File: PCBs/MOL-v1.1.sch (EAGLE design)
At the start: 67 parts, among them IC1 ULN2803, IC2 ULN2803, J1 SERVO 1, J2 SERVO 2, U1 SN74LVC2G04DBV, U2 JOYSTICKPTH, U3 JOYSTICKPTH

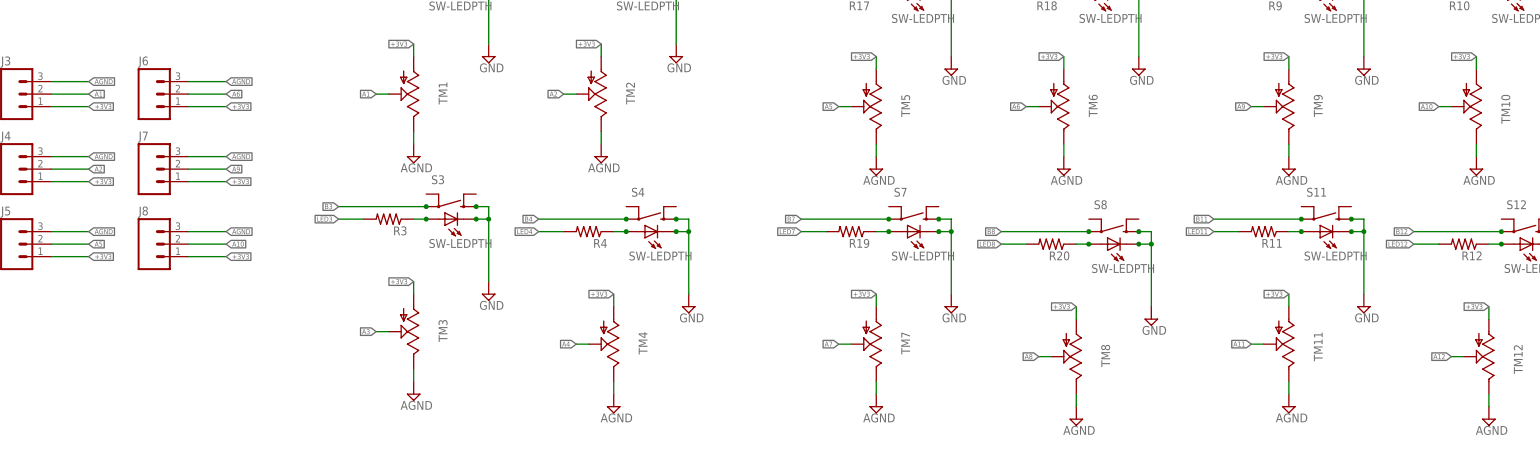
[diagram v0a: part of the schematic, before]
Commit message: signal name changes in MOL PCB v1.1
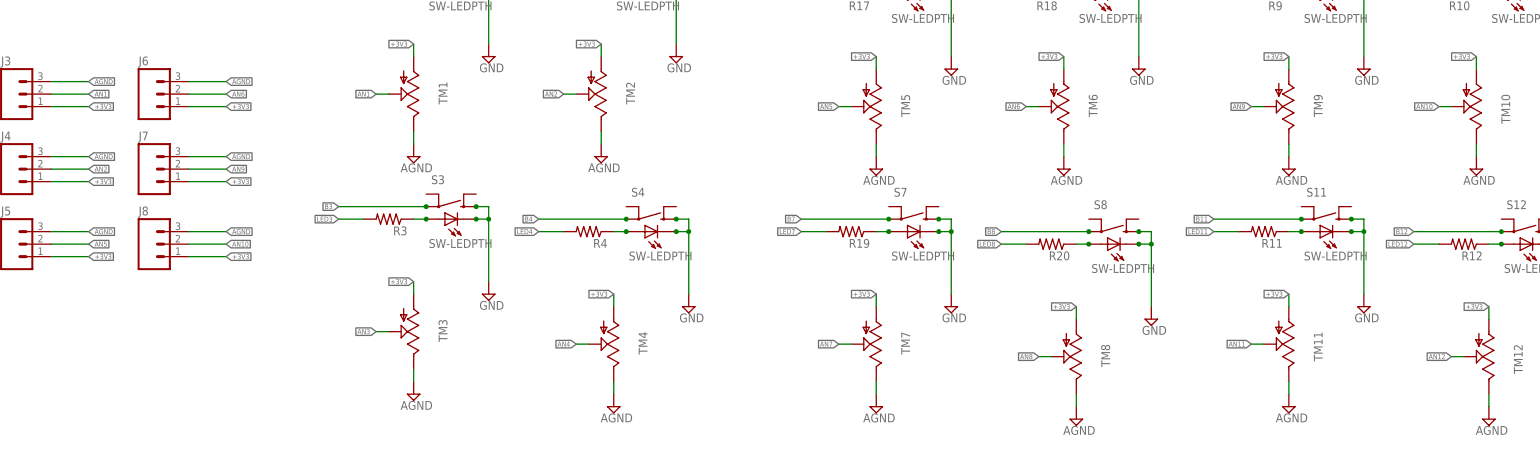
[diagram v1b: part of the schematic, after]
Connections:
- removed net A1: J3.2, TM1.S
- removed net A10: J8.2, TM10.S
- removed net A11: TM11.S
- removed net A12: TM12.S
- removed net A2: J4.2, TM2.S
- removed net A3: TM3.S
- removed net A4: TM4.S
- removed net A5: J5.2, TM5.S
- removed net A6: J6.2, TM6.S
- removed net A7: TM7.S
- removed net A8: TM8.S
- removed net A9: J7.2, TM9.S
- net AN1: now also J3.2, TM1.S
- net AN10: now also J8.2, TM10.S
- net AN11: now also TM11.S
- net AN12: now also TM12.S
- net AN2: now also J4.2, TM2.S
- net AN3: now also TM3.S
- net AN4: now also TM4.S
- net AN5: now also J5.2, TM5.S
- net AN6: now also J6.2, TM6.S
- net AN7: now also TM7.S
- net AN8: now also TM8.S
- net AN9: now also J7.2, TM9.S
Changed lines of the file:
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@@
-</segment>
-</net>
-<net name="A1" class="3">
-<segment>
-<pinref part="TM1" gate="G$1" pin="S"/>
-<wire x1="-83.82" y1="-81.28" x2="-86.36" y2="-81.28" width="0.1524" layer="91"/>
-<label x="-86.36" y="-81.28" size="1.016" layer="95" rot="R180" xref="yes"/>
-</segment>
-<segment>
-<pinref part="J3" gate="G$1" pin="2"/>
-<wire x1="-152.4" y1="-81.28" x2="-144.78" y2="-81.28" width="0.1524" layer="91"/>
-<label x="-144.78" y="-81.28" size="1.016" layer="95" xref="yes"/>
-</segment>
-</net>
-<net name="A2" class="3">
-<segment>
-<pinref part="TM2" gate="G$1" pin="S"/>
-<wire x1="-45.72" y1="-81.28" x2="-48.26" y2="-81.28" width="0.1524" layer="91"/>
-<label x="-48.26" y="-81.28" size="1.016" layer="95" rot="R180" xref="yes"/>
-</segment>
-<segment>
-<pinref part="J4" gate="G$1" pin="2"/>
-<wire x1="-152.4" y1="-96.52" x2="-144.78" y2="-96.52" width="0.1524" layer="91"/>
-<label x="-144.78" y="-96.52" size="1.016" layer="95" xref="yes"/>
-</segment>
-</net>
-<net name="A3" class="3">
-<segment>
-<pinref part="TM3" gate="G$1" pin="S"/>
-<wire x1="-83.82" y1="-129.54" x2="-86.36" y2="-129.54" width="0.1524" layer="91"/>
-<label x="-86.36" y="-129.54" size="1.016" layer="95" rot="R180" xref="yes"/>
-</segment>
-</net>
-<net name="A4" class="3">
-<segment>
-<pinref part="TM4" gate="G$1" pin="S"/>
-<wire x1="-43.18" y1="-132.08" x2="-45.72" y2="-132.08" width="0.1524" layer="91"/>
-<label x="-45.72" y="-132.08" size="1.016" layer="95" rot="R180" xref="yes"/>
-</segment>
-</net>
-<net name="A5" class="3">
-<segment>
-<pinref part="TM5" gate="G$1" pin="S"/>
-<wire x1="10.16" y1="-83.82" x2="7.62" y2="-83.82" width="0.1524" layer="91"/>
-<label x="7.62" y="-83.82" size="1.016" layer="95" rot="R180" xref="yes"/>
-</segment>
-<segment>
-<pinref part="J5" gate="G$1" pin="2"/>
-<wire x1="-152.4" y1="-111.76" x2="-144.78" y2="-111.76" width="0.1524" layer="91"/>
-<label x="-144.78" y="-111.76" size="1.016" layer="95" xref="yes"/>
-</segment>
-</net>
-<net name="A6" class="3">
-<segment>
-<pinref part="TM6" gate="G$1" pin="S"/>
-<wire x1="48.26" y1="-83.82" x2="45.72" y2="-83.82" width="0.1524" layer="91"/>
-<label x="45.72" y="-83.82" size="1.016" layer="95" rot="R180" xref="yes"/>
-</segment>
-<segment>
-<pinref part="J6" gate="G$1" pin="2"/>
-<wire x1="-124.46" y1="-81.28" x2="-116.84" y2="-81.28" width="0.1524" layer="91"/>
-<label x="-116.84" y="-81.28" size="1.016" layer="95" xref="yes"/>
-</segment>
-</net>
-<net name="A7" class="3">
-<segment>
-<pinref part="TM7" gate="G$1" pin="S"/>
-<wire x1="10.16" y1="-132.08" x2="7.62" y2="-132.08" width="0.1524" layer="91"/>
-<label x="7.62" y="-132.08" size="1.016" layer="95" rot="R180" xref="yes"/>
-</segment>
-</net>
-<net name="A10" class="3">
-<segment>
-<pinref part="TM10" gate="G$1" pin="S"/>
-<wire x1="132.08" y1="-83.82" x2="129.54" y2="-83.82" width="0.1524" layer="91"/>
-<label x="129.54" y="-83.82" size="1.016" layer="95" rot="R180" xref="yes"/>
-</segment>
-<segment>
-<pinref part="J8" gate="G$1" pin="2"/>
-<wire x1="-124.46" y1="-111.76" x2="-116.84" y2="-111.76" width="0.1524" layer="91"/>
-<label x="-116.84" y="-111.76" size="1.016" layer="95" xref="yes"/>
-</segment>
-</net>
-<net name="A11" class="3">
-<segment>
-<pinref part="TM11" gate="G$1" pin="S"/>
-<wire x1="93.98" y1="-132.08" x2="91.44" y2="-132.08" width="0.1524" layer="91"/>
-<label x="91.44" y="-132.08" size="1.016" layer="95" rot="R180" xref="yes"/>
-</segment>
-</net>
-<net name="A12" class="3">
-<segment>
-<pinref part="TM12" gate="G$1" pin="S"/>
-<wire x1="134.62" y1="-134.62" x2="132.08" y2="-134.62" width="0.1524" layer="91"/>
-<label x="132.08" y="-134.62" size="1.016" layer="95" rot="R180" xref="yes"/>
 </segment>
 </net>
@@
 </segment>
 </net>
-<net name="A8" class="3">
-<segment>
-<pinref part="TM8" gate="G$1" pin="S"/>
-<wire x1="50.8" y1="-134.62" x2="48.26" y2="-134.62" width="0.1524" layer="91"/>
-<label x="48.26" y="-134.62" size="1.016" layer="95" rot="R180" xref="yes"/>
-</segment>
-</net>
-<net name="A9" class="3">
-<segment>
-<pinref part="TM9" gate="G$1" pin="S"/>
-<wire x1="93.98" y1="-83.82" x2="91.44" y2="-83.82" width="0.1524" layer="91"/>
-<label x="91.44" y="-83.82" size="1.016" layer="95" rot="R180" xref="yes"/>
-</segment>
-<segment>
-<pinref part="J7" gate="G$1" pin="2"/>
-<wire x1="-124.46" y1="-96.52" x2="-116.84" y2="-96.52" width="0.1524" layer="91"/>
-<label x="-116.84" y="-96.52" size="1.016" layer="95" xref="yes"/>
-</segment>
-</net>
 <net name="N$2" class="0">
 <segment>
@@
 <label x="-78.74" y="157.48" size="1.016" layer="95" rot="R180" xref="yes"/>
 </segment>
+<segment>
+<pinref part="TM1" gate="G$1" pin="S"/>
+<wire x1="-83.82" y1="-81.28" x2="-86.36" y2="-81.28" width="0.1524" layer="91"/>
+<label x="-86.36" y="-81.28" size="1.016" layer="95" rot="R180" xref="yes"/>
+</segment>
+<segment>
+<pinref part="J3" gate="G$1" pin="2"/>
+<wire x1="-152.4" y1="-81.28" x2="-144.78" y2="-81.28" width="0.1524" layer="91"/>
+<label x="-144.78" y="-81.28" size="1.016" layer="95" xref="yes"/>
+</segment>
 </net>
 <net name="AN2" class="3">
@@
 <label x="-78.74" y="154.94" size="1.016" layer="95" rot="R180" xref="yes"/>
 </segment>
+<segment>
+<pinref part="TM2" gate="G$1" pin="S"/>
+<wire x1="-45.72" y1="-81.28" x2="-48.26" y2="-81.28" width="0.1524" layer="91"/>
+<label x="-48.26" y="-81.28" size="1.016" layer="95" rot="R180" xref="yes"/>
+</segment>
+<segment>
+<pinref part="J4" gate="G$1" pin="2"/>
+<wire x1="-152.4" y1="-96.52" x2="-144.78" y2="-96.52" width="0.1524" layer="91"/>
+<label x="-144.78" y="-96.52" size="1.016" layer="95" xref="yes"/>
+</segment>
 </net>
 <net name="AN3" class="3">
@@
 <label x="-78.74" y="152.4" size="1.016" layer="95" rot="R180" xref="yes"/>
 </segment>
+<segment>
+<pinref part="TM3" gate="G$1" pin="S"/>
+<wire x1="-83.82" y1="-129.54" x2="-86.36" y2="-129.54" width="0.1524" layer="91"/>
+<label x="-86.36" y="-129.54" size="1.016" layer="95" rot="R180" xref="yes"/>
+</segment>
 </net>
 <net name="AN4" class="3">
@@
 <label x="-78.74" y="109.22" size="1.016" layer="95" rot="R180" xref="yes"/>
 </segment>
+<segment>
+<pinref part="TM4" gate="G$1" pin="S"/>
+<wire x1="-43.18" y1="-132.08" x2="-45.72" y2="-132.08" width="0.1524" layer="91"/>
+<label x="-45.72" y="-132.08" size="1.016" layer="95" rot="R180" xref="yes"/>
+</segment>
 </net>
 <net name="AN5" class="3">
@@
 <label x="-78.74" y="106.68" size="1.016" layer="95" rot="R180" xref="yes"/>
 </segment>
+<segment>
+<pinref part="TM5" gate="G$1" pin="S"/>
+<wire x1="10.16" y1="-83.82" x2="7.62" y2="-83.82" width="0.1524" layer="91"/>
+<label x="7.62" y="-83.82" size="1.016" layer="95" rot="R180" xref="yes"/>
+</segment>
+<segment>
+<pinref part="J5" gate="G$1" pin="2"/>
+<wire x1="-152.4" y1="-111.76" x2="-144.78" y2="-111.76" width="0.1524" layer="91"/>
+<label x="-144.78" y="-111.76" size="1.016" layer="95" xref="yes"/>
+</segment>
 </net>
 <net name="AN6" class="3">
@@
 <label x="-78.74" y="104.14" size="1.016" layer="95" rot="R180" xref="yes"/>
 </segment>
+<segment>
+<pinref part="TM6" gate="G$1" pin="S"/>
+<wire x1="48.26" y1="-83.82" x2="45.72" y2="-83.82" width="0.1524" layer="91"/>
+<label x="45.72" y="-83.82" size="1.016" layer="95" rot="R180" xref="yes"/>
+</segment>
+<segment>
+<pinref part="J6" gate="G$1" pin="2"/>
+<wire x1="-124.46" y1="-81.28" x2="-116.84" y2="-81.28" width="0.1524" layer="91"/>
+<label x="-116.84" y="-81.28" size="1.016" layer="95" xref="yes"/>
+</segment>
 </net>
 <net name="AN7" class="3">
@@
 <label x="-78.74" y="101.6" size="1.016" layer="95" rot="R180" xref="yes"/>
 </segment>
+<segment>
+<pinref part="TM7" gate="G$1" pin="S"/>
+<wire x1="10.16" y1="-132.08" x2="7.62" y2="-132.08" width="0.1524" layer="91"/>
+<label x="7.62" y="-132.08" size="1.016" layer="95" rot="R180" xref="yes"/>
+</segment>
 </net>
 <net name="AN8" class="3">
@@
 <label x="0" y="106.68" size="1.016" layer="95" xref="yes"/>
 </segment>
+<segment>
+<pinref part="TM8" gate="G$1" pin="S"/>
+<wire x1="50.8" y1="-134.62" x2="48.26" y2="-134.62" width="0.1524" layer="91"/>
+<label x="48.26" y="-134.62" size="1.016" layer="95" rot="R180" xref="yes"/>
+</segment>
 </net>
 <net name="AN9" class="3">
@@
 <label x="0" y="154.94" size="1.016" layer="95" xref="yes"/>
 </segment>
+<segment>
+<pinref part="TM9" gate="G$1" pin="S"/>
+<wire x1="93.98" y1="-83.82" x2="91.44" y2="-83.82" width="0.1524" layer="91"/>
+<label x="91.44" y="-83.82" size="1.016" layer="95" rot="R180" xref="yes"/>
+</segment>
+<segment>
+<pinref part="J7" gate="G$1" pin="2"/>
+<wire x1="-124.46" y1="-96.52" x2="-116.84" y2="-96.52" width="0.1524" layer="91"/>
+<label x="-116.84" y="-96.52" size="1.016" layer="95" xref="yes"/>
+</segment>
 </net>
 <net name="AN10" class="3">
@@
 <label x="0" y="157.48" size="1.016" layer="95" xref="yes"/>
 </segment>
+<segment>
+<pinref part="TM10" gate="G$1" pin="S"/>
+<wire x1="132.08" y1="-83.82" x2="129.54" y2="-83.82" width="0.1524" layer="91"/>
+<label x="129.54" y="-83.82" size="1.016" layer="95" rot="R180" xref="yes"/>
+</segment>
+<segment>
+<pinref part="J8" gate="G$1" pin="2"/>
+<wire x1="-124.46" y1="-111.76" x2="-116.84" y2="-111.76" width="0.1524" layer="91"/>
+<label x="-116.84" y="-111.76" size="1.016" layer="95" xref="yes"/>
+</segment>
 </net>
 <net name="AN11" class="3">
@@
 <label x="0" y="165.1" size="1.016" layer="95" xref="yes"/>
 </segment>
+<segment>
+<pinref part="TM11" gate="G$1" pin="S"/>
+<wire x1="93.98" y1="-132.08" x2="91.44" y2="-132.08" width="0.1524" layer="91"/>
+<label x="91.44" y="-132.08" size="1.016" layer="95" rot="R180" xref="yes"/>
+</segment>
 </net>
 <net name="AN12" class="3">
@@
 <label x="0" y="167.64" size="1.016" layer="95" xref="yes"/>
 </segment>
-</net>
+<segment>
+<pinref part="TM12" gate="G$1" pin="S"/>
+<wire x1="134.62" y1="-134.62" x2="132.08" y2="-134.62" width="0.1524" layer="91"/>
+<label x="132.08" y="-134.62" size="1.016" layer="95" rot="R180" xref="yes"/>
+</segment>
+</net>
